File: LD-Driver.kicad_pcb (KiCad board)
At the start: 2 copper layers, 107.5 x 72 mm, 134 parts, among them J1 BASYS3, J2 BUTTERFLY, J3 Barrel_Jack_Switch, J4 SELECTOR, J5 Conn_02x07_Counter_Clockwise, J6 Conn_01x02, Q1 RJK0355DSP, Q10 RJK0355DSP, Q2 RJK0355DSP, Q3 SiRC18DP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

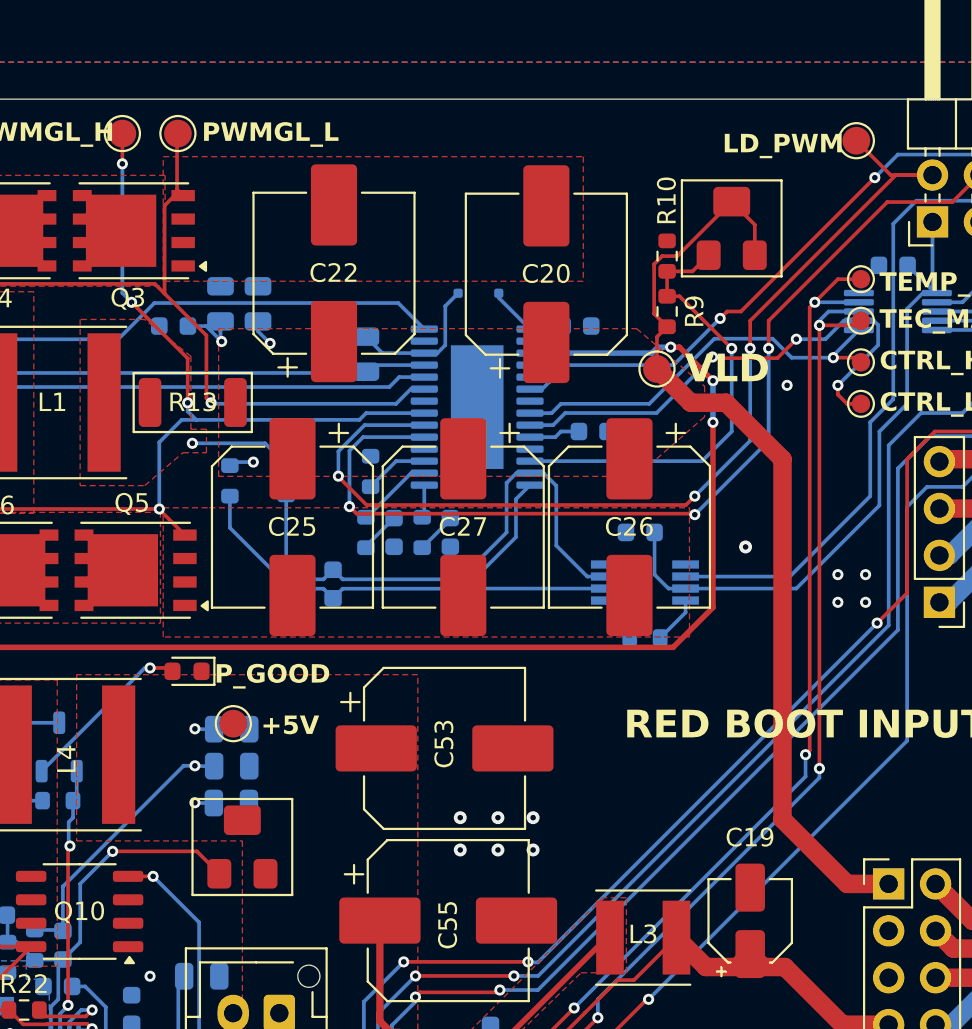
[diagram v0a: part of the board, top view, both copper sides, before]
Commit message: fix: small corrections to the pcb, added PNs and store link to mouser for each component
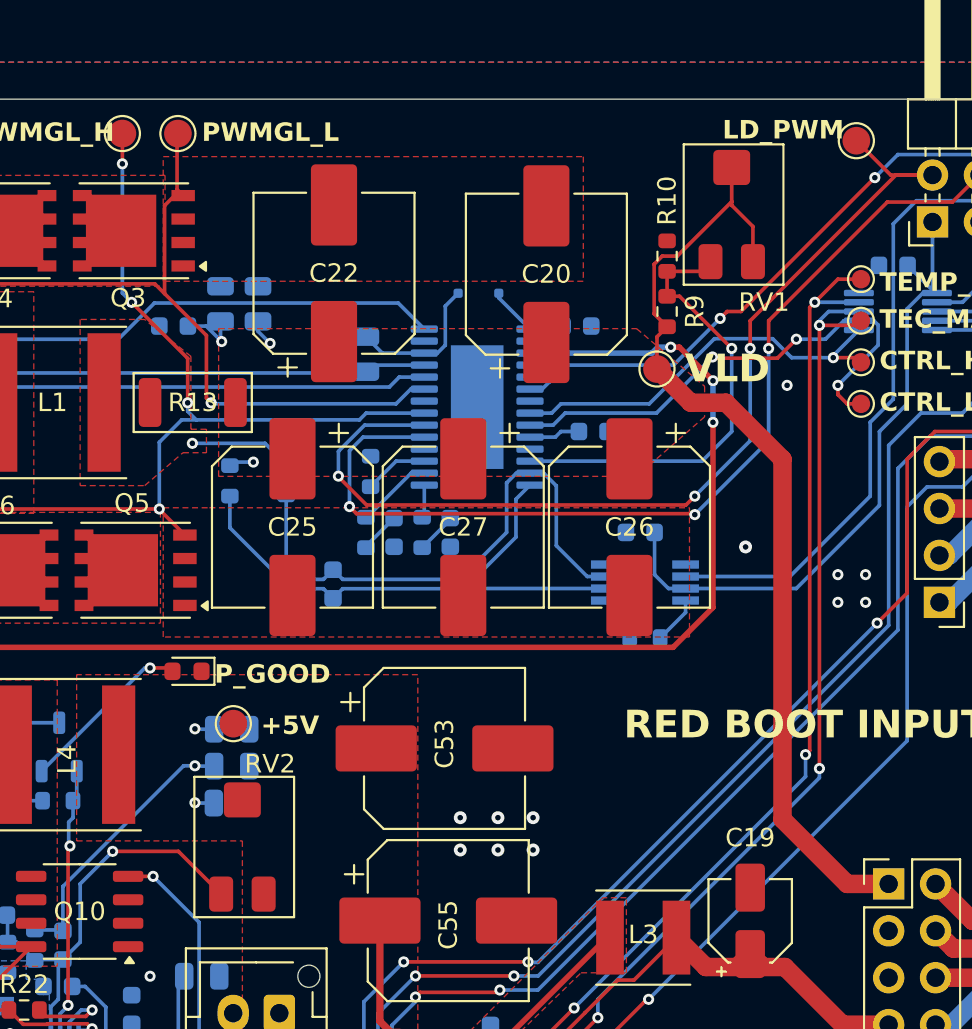
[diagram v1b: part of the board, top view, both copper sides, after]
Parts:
- D3: value 1PS76SB21 -> BAT54
- J5: value Conn_02x07_Counter_Clockwise -> SELECTOR_2
- J6: value Conn_01x02 -> 5V EXT
- R10: value 10K -> 1k
- R12: value 50m -> 200m
- R13: value 25m -> 50m
- R26: value 100k -> 5k6
- R27: value 10k -> 1k
- R7, R8: value 800k -> 806k
- R9: value 100k -> 2k2
- RV1: value 100k -> 1k; footprint PCM_Potentiometer_SMD_AKL:Potentiometer_Bourns_3214W_Vertical -> PCM_Potentiometer_SMD_AKL:Potentiometer_Bourns_3224X_Vertical
- RV2: value 100k -> 10k; footprint PCM_Potentiometer_SMD_AKL:Potentiometer_Bourns_3214W_Vertical -> PCM_Potentiometer_SMD_AKL:Potentiometer_Bourns_3224X_Vertical
- moved RV1 0.75 mm to (125.0, 58.2)
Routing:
- net /Driver/LD: track 56.8 -> 59.0 mm
- net /Power/FB: track 22.3 -> 22.8 mm
